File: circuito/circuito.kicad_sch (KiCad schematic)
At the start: 0 parts

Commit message: modificando o circuito
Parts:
- added A1: ESP32_DevKit, PCM_SL_Development_Boards:DOIT_ESP32_DEVKIT_36Pins, symbol PCM_SL_Development_Board:ESP32_DevKit_V1_DOIT_36GPIOs
- added R1: 4,7 KΩ, Resistor_THT:R_Axial_DIN0207_L6.3mm_D2.5mm_P10.16mm_Horizontal, symbol PCM_SL_Resistors:Resistor
- added U1: DS18B20, Package_TO_SOT_THT:TO-92_Inline, symbol Sensor_Temperature:DS18B20
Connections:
- new net: R1.1, U1.3 (V_{DD})
- new net: R1.2, U1.2 (DQ)
- new net GND: A1.35 (GND), U1.1 (GND)

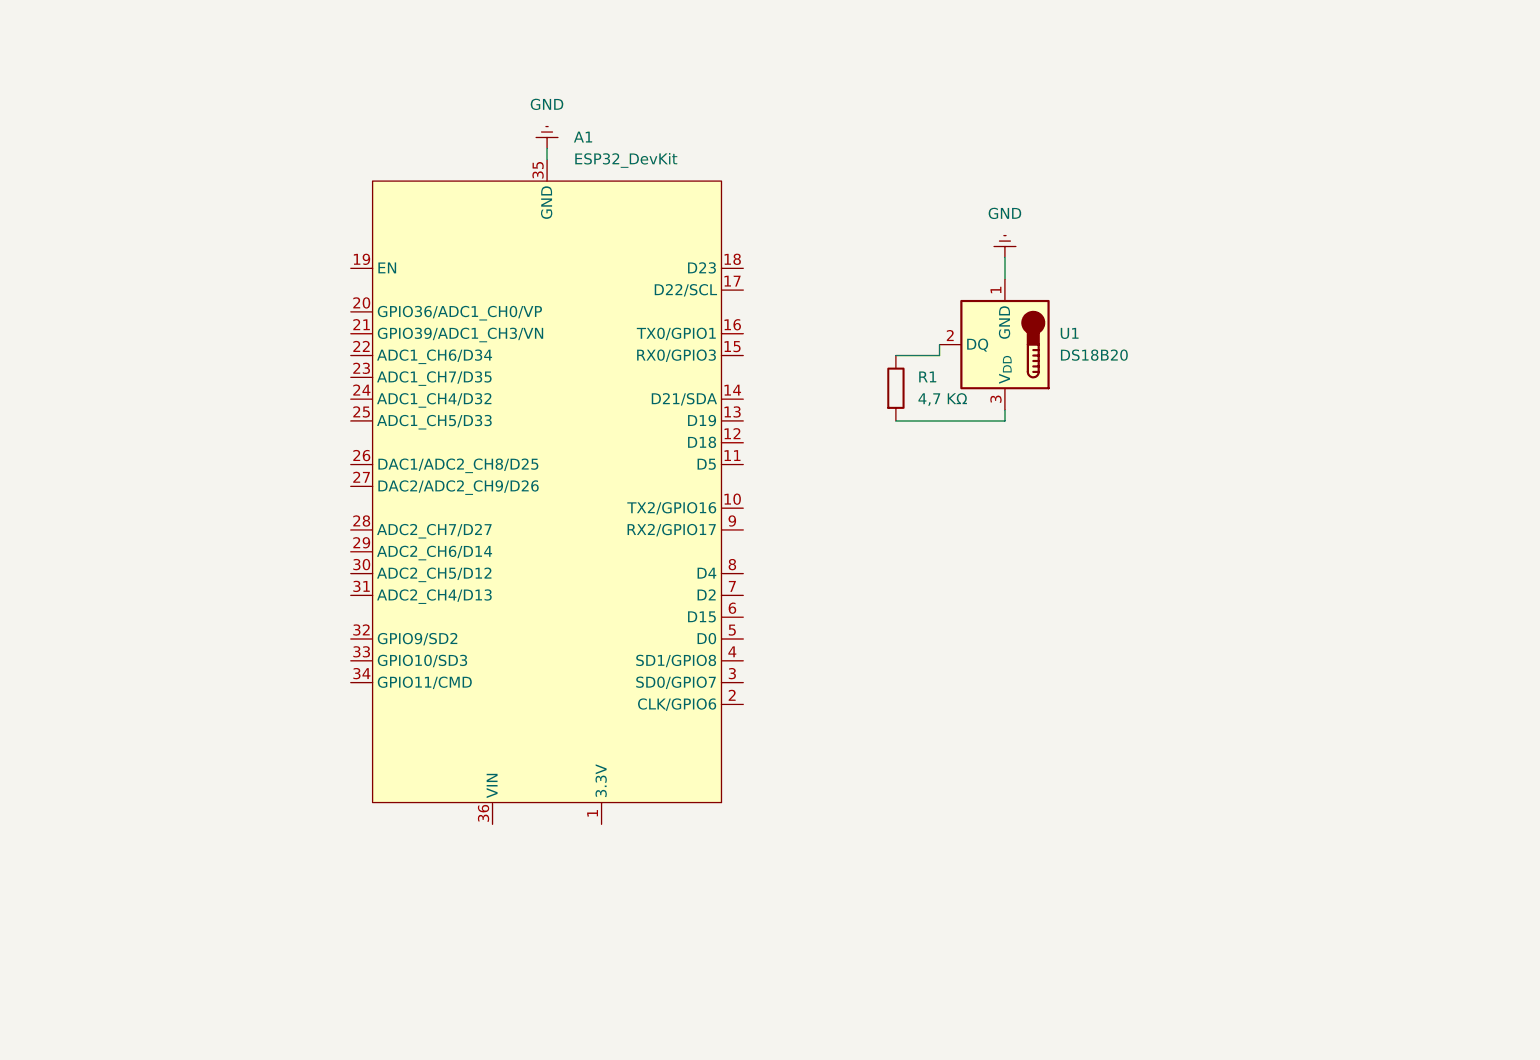
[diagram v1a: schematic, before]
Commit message: iniciando logica de controle de temperatura
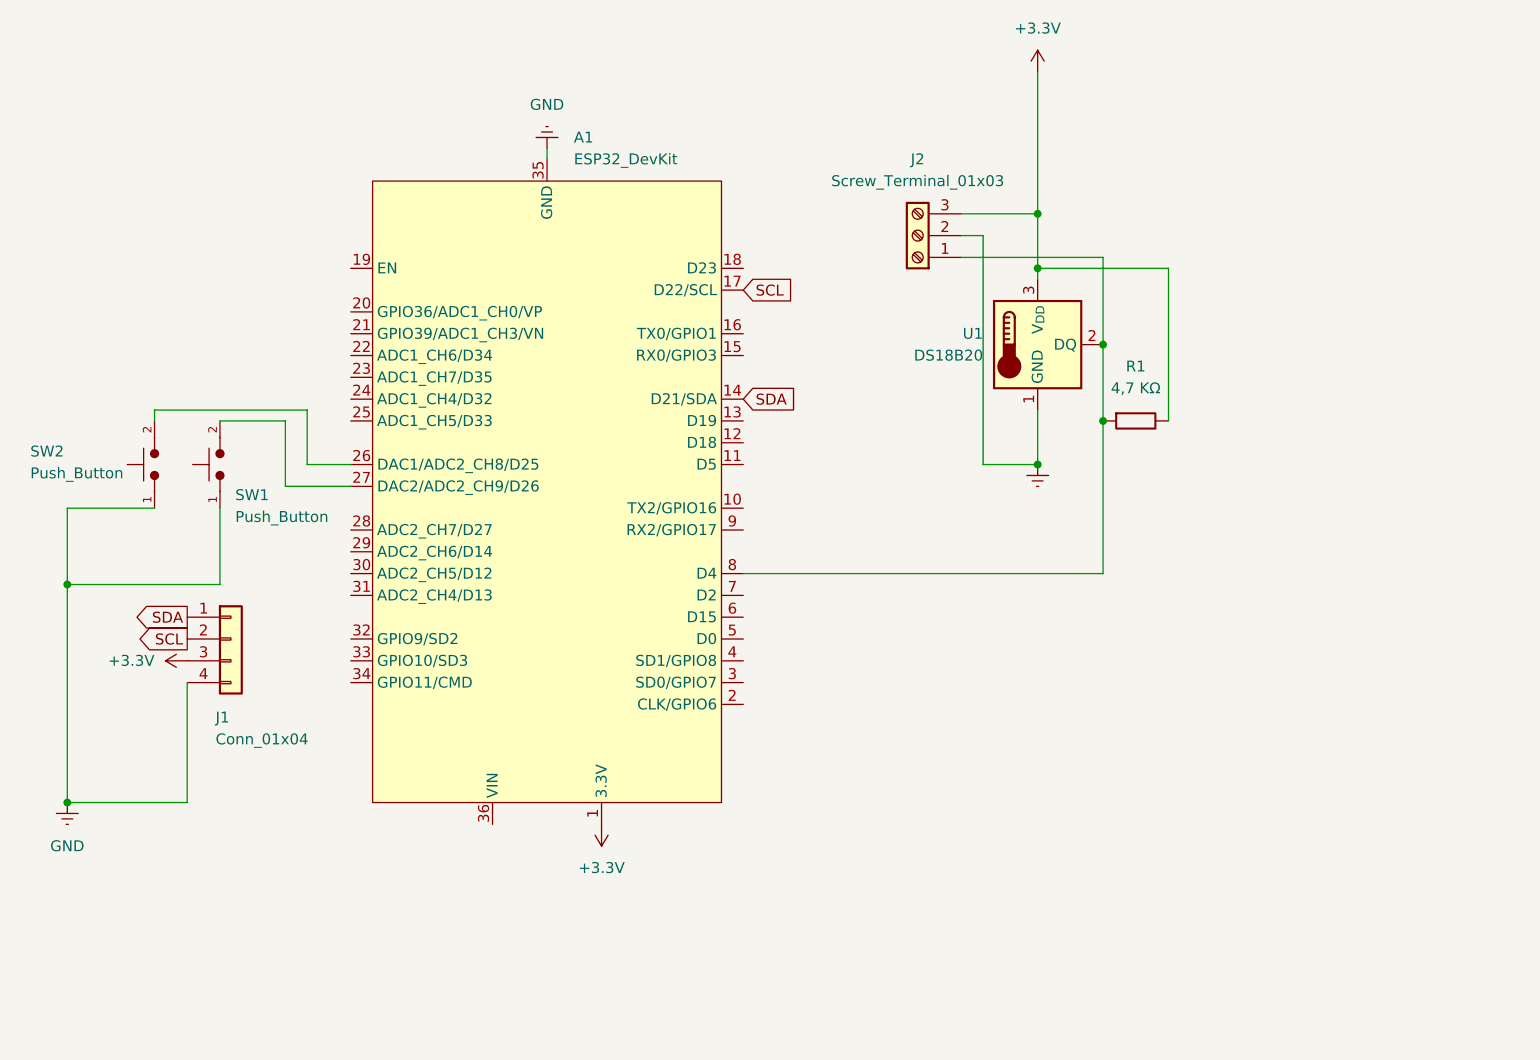
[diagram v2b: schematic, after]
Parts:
- added J1: Conn_01x04, Connector:FanPinHeader_1x04_P2.54mm_Vertical, symbol Connector_Generic:Conn_01x04
- added J2: Screw_Terminal_01x03, TerminalBlock:TerminalBlock_MaiXu_MX126-5.0-03P_1x03_P5.00mm, symbol Connector:Screw_Terminal_01x03
- added SW1, SW2: Push_Button, Button_Switch_THT:SW_PUSH_6mm, symbol PCM_SL_Devices:Push_Button
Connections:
- net GND: now also J1.4 (Pin_4), J2.2 (Pin_2), SW1.1, SW2.1
- net at R1.1: now also A1.8 (D4), U1.2 (DQ), J2.1 (Pin_1); no longer U1.3 (V_{DD})
- net +3.3V: now reaches R1.2
- net +3.3V: now also A1.1 (3.3V), U1.3 (V_{DD}), J1.3 (Pin_3), J2.3 (Pin_3); no longer U1.2 (DQ)
- net SDA: now reaches A1.14 (D21/SDA)
- net SDA: now also J1.1 (Pin_1)
- net SCL: now reaches A1.17 (D22/SCL)
- net SCL: now also J1.2 (Pin_2)
- net at A1.26 (DAC1/ADC2_CH8/D25): now also SW2.2
- net at A1.27 (DAC2/ADC2_CH9/D26): now also SW1.2
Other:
- moved on the sheet: R1, U1

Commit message: atualizando circuito
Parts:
- added P2: Conn_Plug_3P_Protected, symbol Connector:Conn_Plug_3P_Protected
- added U3: S216S01, Package_SIP:SIP4_Sharp-SSR_P7.62mm_Straight, symbol Relay_SolidState:S216S01
- SW1: value Push_Button -> Up_Button
- SW2: value Push_Button -> Down_Button
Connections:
- net +3.3V: no longer J1.3 (Pin_3)
- net GND: now also U3.4
- net at SW2.2: now also A1.28 (ADC2_CH7/D27); no longer A1.26 (DAC1/ADC2_CH8/D25)
- net at A1.11 (D5): now also U3.3
- net 5V: now reaches A1.36 (VIN)
- net 5V: now also J1.3 (Pin_3)
- new net: P2.2 (N), U3.1
- new net AC: P2.1 (L), U3.2
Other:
- moved on the sheet: SW2
